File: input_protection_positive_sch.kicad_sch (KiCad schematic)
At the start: 27 parts, among them Q1 SQM120P06, Q2 SQM120P06, U1 ADM1270

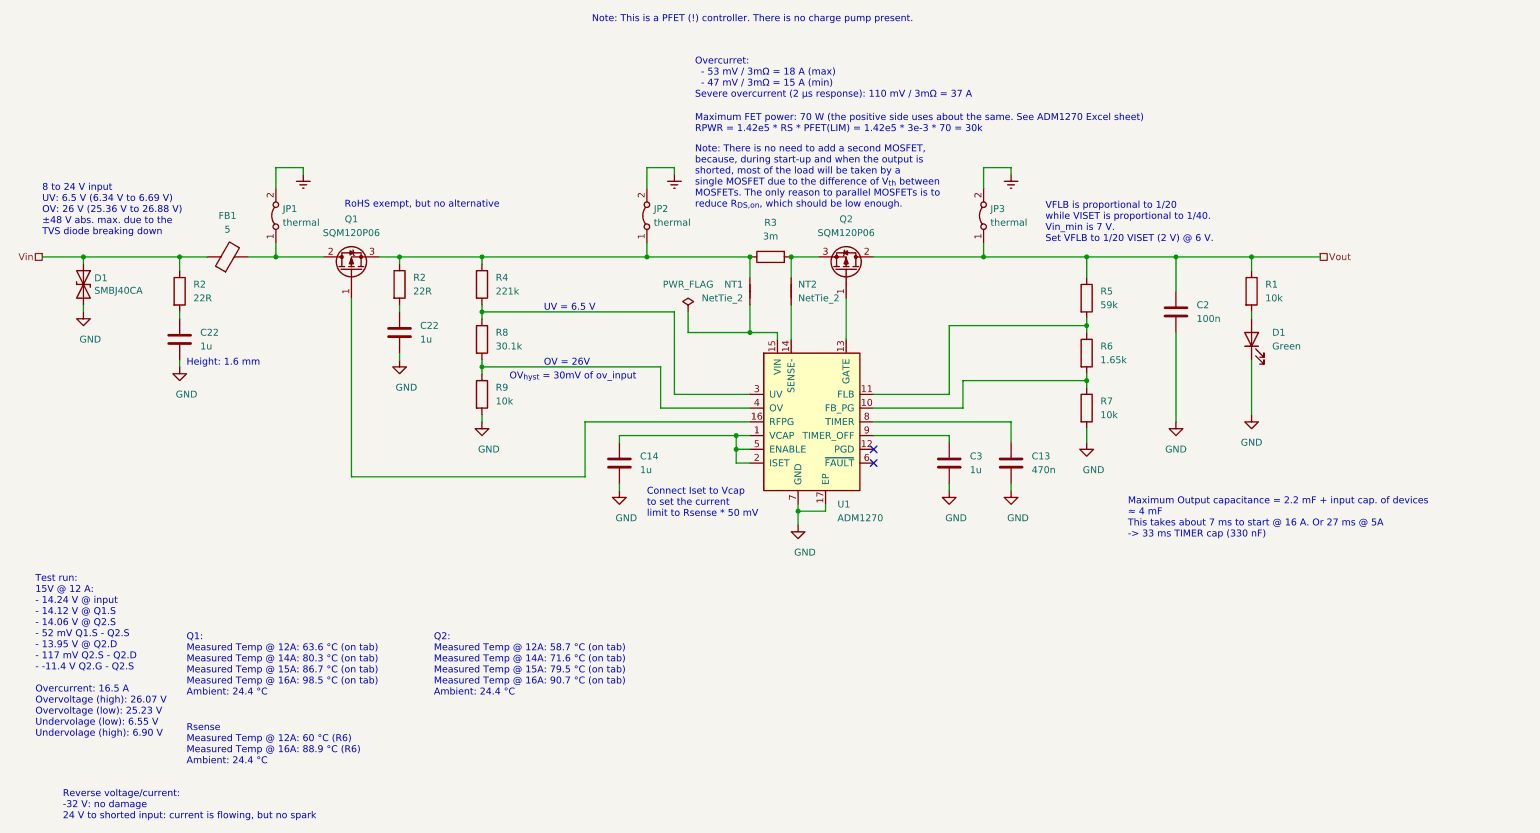
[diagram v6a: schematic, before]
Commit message: Added test points
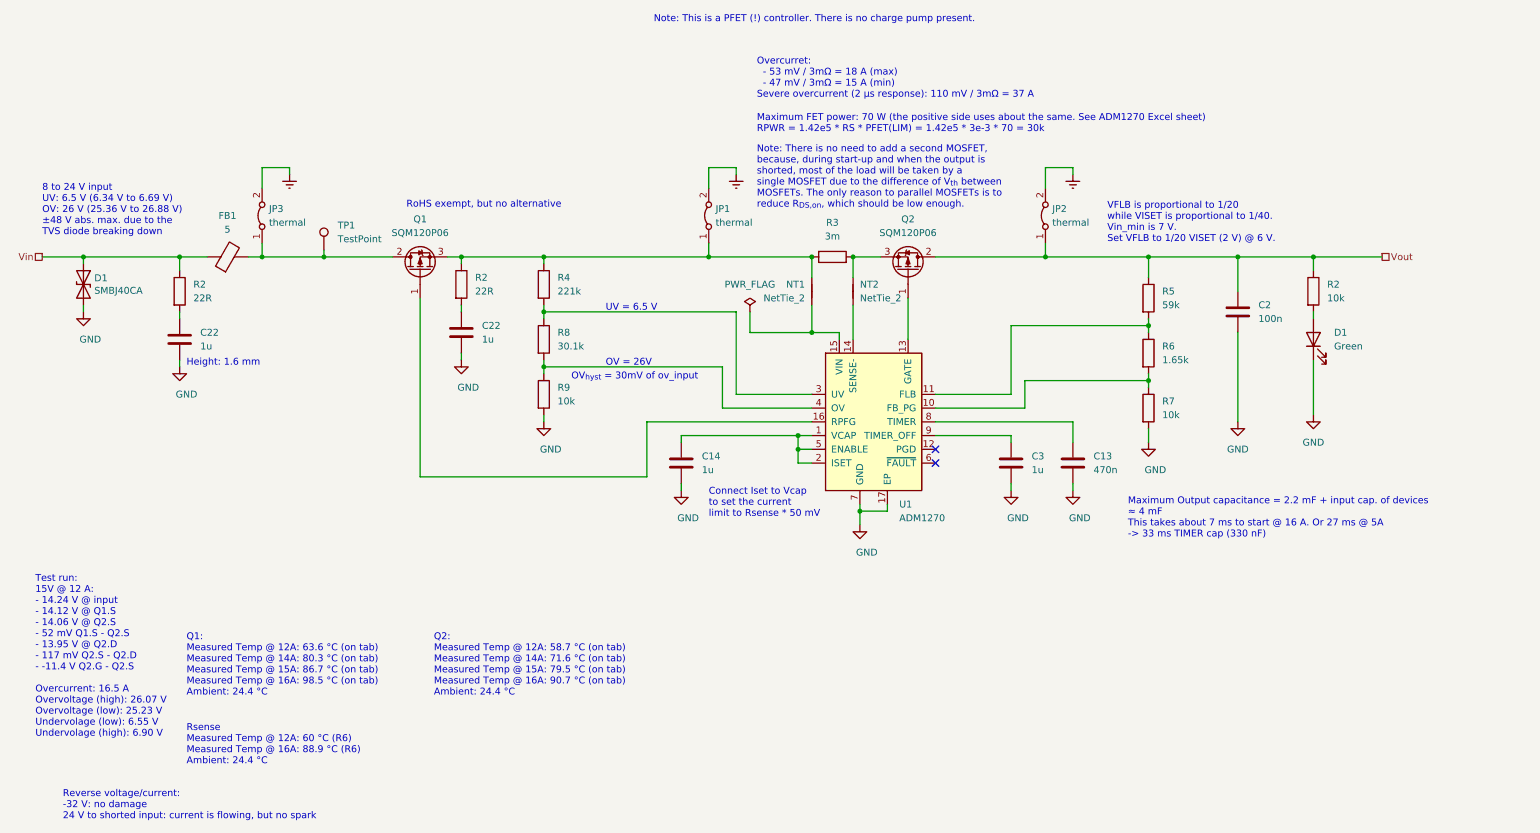
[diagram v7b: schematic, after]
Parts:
- added TP1: TestPoint, TestPoint:TestPoint_Pad_D1.5mm, symbol Connector:TestPoint
- renumbered JP2 to JP1, JP3 to JP2, JP1 to JP3, R1 to R2
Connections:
- net at FB1.2, JP3.1 (A), Q1.2 (D): now also TP1.1
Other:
- moved on the sheet: C13, C14, C2, C22, C3, D1, JP1, JP2, JP3, NT1, NT2, Q1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

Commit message: Cleaned up BOM
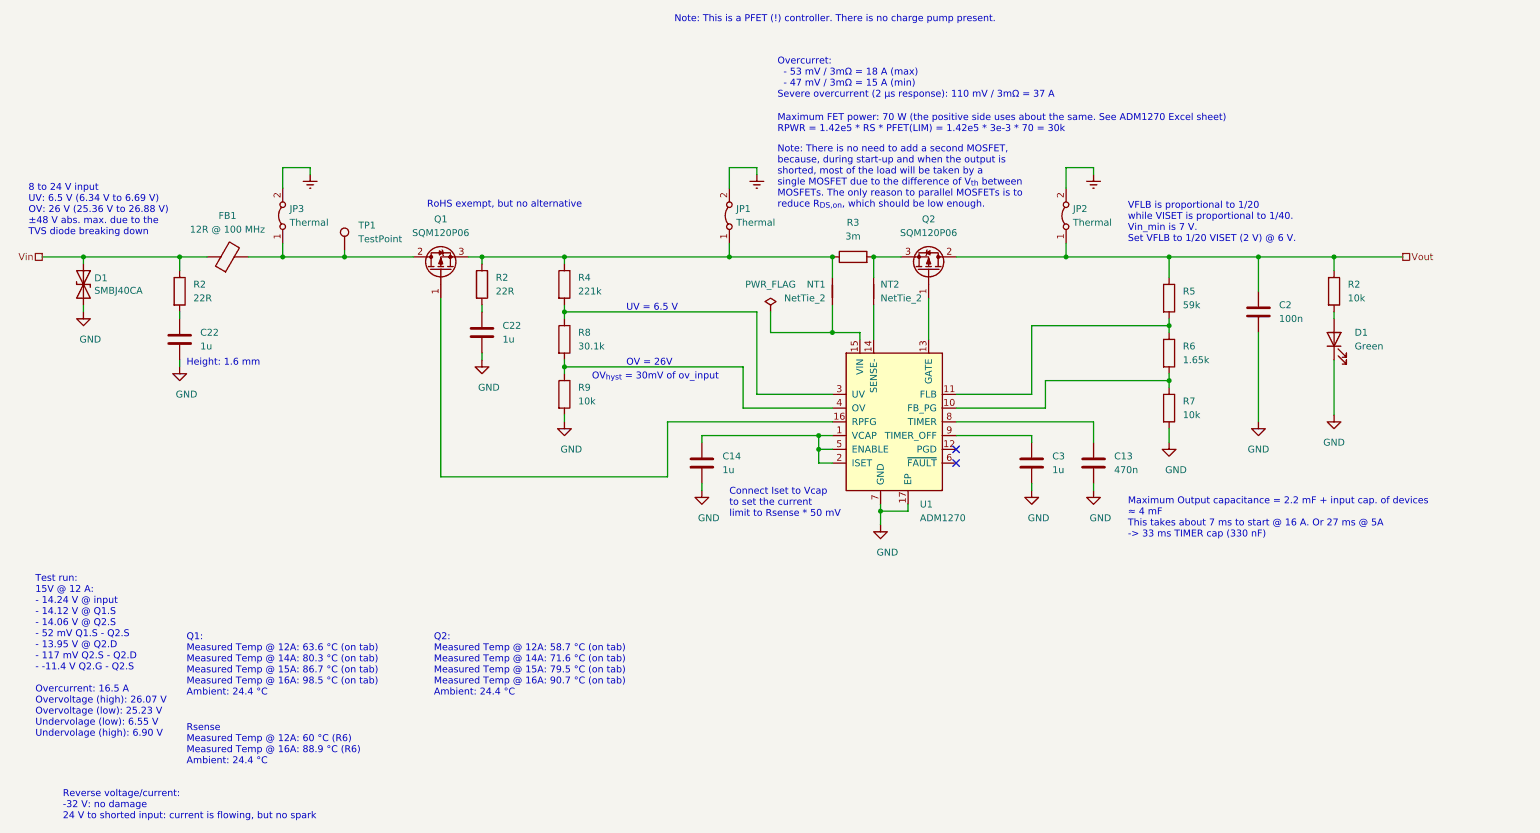
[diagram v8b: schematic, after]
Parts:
- FB1: value 5 -> 12R @ 100 MHz
- JP1, JP2, JP3: value thermal -> Thermal
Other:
- moved on the sheet: C13, C14, C2, C22, C3, D1, JP1, JP2, JP3, NT1, NT2, Q1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
